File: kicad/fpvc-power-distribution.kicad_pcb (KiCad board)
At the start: 2 copper layers, 100.3 x 80.8 mm, 44 parts, among them J10 Load Drivers, J4 PLC_In, J5 PLC_Out, J7 Vout_Screen, J8 PG, J9 GPIO, Q1 IRLB8314, Q2 IRLB8314, Q3 IRLB8314, U1 D42V110F12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

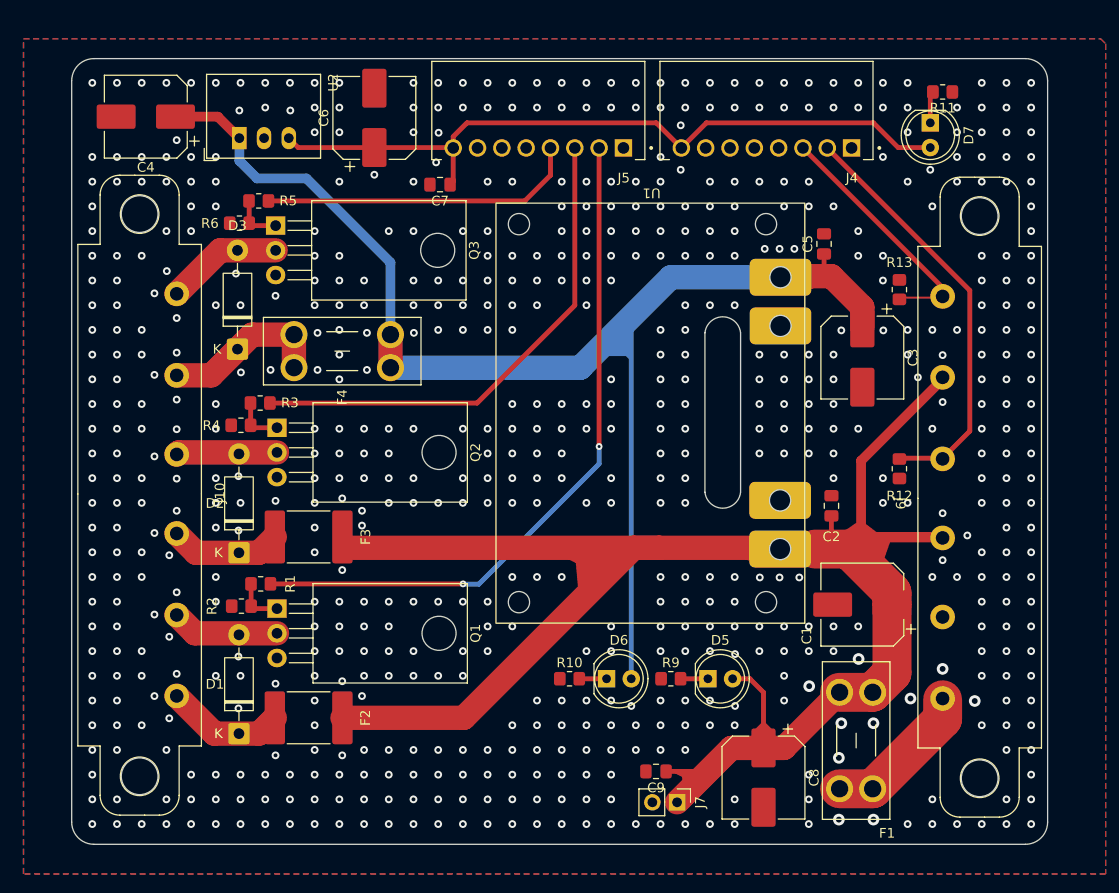
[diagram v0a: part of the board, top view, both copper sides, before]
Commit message: feat: Update silkscreen
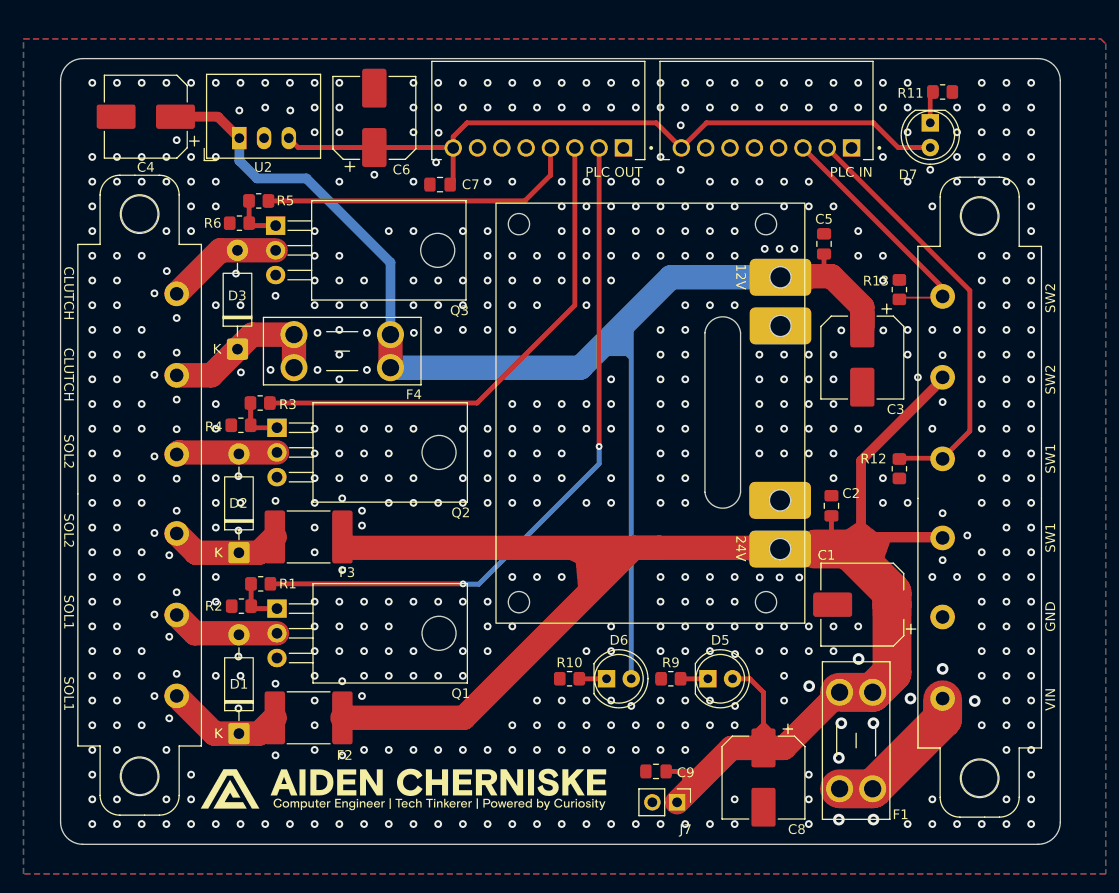
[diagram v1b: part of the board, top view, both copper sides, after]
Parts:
- PLC IN: renamed from J4
- PLC OUT: renamed from J5
- renumbered J9 to GPIO
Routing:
- net GND: vias 665 -> 631
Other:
- board size 100.3 x 80.8 mm -> 102.8 x 80.8 mm
- board text added: "12V"
- board text added: "24V"
- board text added: "CLUTCH"
- board text added: "GND"
- board text added: "SOL1"
- board text added: "SOL2"
- board text added: "SW1"
- board text added: "SW2"
- board text added: "VIN"

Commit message: feat: Update 3d models
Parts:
- removed D4: Fault_Ind, LED_THT:LED_D5.0mm
- removed J8: PG, Connector_PinHeader_2.00mm:PinHeader_1x01_P2.00mm_Vertical
- removed R7: 100k, Resistor_SMD:R_0805_2012Metric_Pad1.20x1.40mm_HandSolder
- removed R8: 680, Resistor_SMD:R_0805_2012Metric_Pad1.20x1.40mm_HandSolder

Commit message: fix: Replace 2.54mm pitch pin header with 3.5mm terminal block for screen power connections
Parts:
- added D4: Fault_Ind, LED_THT:LED_D5.0mm, F.Cu at (1.97, 3.23)
- added J8: PG, Connector_PinHeader_2.00mm:PinHeader_1x01_P2.00mm_Vertical, F.Cu at (9.01, 7.42)
- added R7: 100k, Resistor_SMD:R_0805_2012Metric_Pad1.20x1.40mm_HandSolder, F.Cu at (9.36, 0.97)
- added R8: 680, Resistor_SMD:R_0805_2012Metric_Pad1.20x1.40mm_HandSolder, F.Cu at (9.36, 3.92)
- J4: renamed from PLC IN
- J5: renamed from PLC OUT
- J7: footprint Connector_PinHeader_2.54mm:PinHeader_1x02_P2.54mm_Vertical -> TerminalBlock_4Ucon:TerminalBlock_4Ucon_1x02_P3.50mm_Vertical
- moved C9 6.30 mm to (238.3, 153.9), turned to -90 degrees
- moved J7 2.07 mm to (234.3, 151.7), turned to 180 degrees
- renumbered GPIO to J9
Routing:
- net 24V: track 185.2 -> 180.8 mm

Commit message: style: Update pcb editor information and clean up file
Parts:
- removed D4: Fault_Ind, LED_THT:LED_D5.0mm
- removed J8: PG, Connector_PinHeader_2.00mm:PinHeader_1x01_P2.00mm_Vertical
- removed R7: 100k, Resistor_SMD:R_0805_2012Metric_Pad1.20x1.40mm_HandSolder
- removed R8: 680, Resistor_SMD:R_0805_2012Metric_Pad1.20x1.40mm_HandSolder
- moved C1 128.1 mm to (141.1, 73.1)
- moved C3 128.1 mm to (141.1, 47.7)
- moved C4 128.1 mm to (67.4, 23.0)
- moved C8 128.1 mm to (130.9, 90.9)
- moved C9 128.1 mm to (125.2, 93.6)
- moved D1 128.1 mm to (77.0, 86.4)
- moved D2 128.1 mm to (77.0, 67.8)
- moved D3 128.1 mm to (76.9, 46.9)
- moved D5 128.1 mm to (125.2, 80.7)
- moved D7 128.1 mm to (148.1, 23.6)
- moved F2 128.1 mm to (84.2, 84.8)
- moved F3 128.1 mm to (84.2, 66.2)
- moved F4 128.1 mm to (92.6, 48.8)
- moved J10 128.1 mm to (67.3, 61.7)
- moved J9 128.1 mm to (152.6, 62.2)
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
